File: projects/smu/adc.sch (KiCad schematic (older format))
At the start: 30 parts, among them P301 CONN_01X15, P302 CONN_01X03, U301 LM741, U304 LM741, U305 LM311N, U8 DG444, U9 LM741

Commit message: pulled out the connectors to the top sheet
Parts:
- removed P301: CONN_01X15, Pin_Headers:Pin_Header_Straight_1x15, symbol CONN_01X15
- removed P302: CONN_01X03, Pin_Headers:Pin_Header_Straight_1x03, symbol CONN_01X03
- added R307, R308: R, symbol R
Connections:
- wire segments 86 -> 69
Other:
- moved on the sheet: R306, U305
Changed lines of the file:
@@
 Text GLabel 2450 2900 0    60   Input ~ 0
 AGND
-Text GLabel 1750 800  2    60   Input ~ 0
-+VE
-Text GLabel 1750 900  2    60   Input ~ 0
-AGND
-Text GLabel 1750 1000 2    60   Input ~ 0
--VE
 Text GLabel 1650 2700 0    60   Input ~ 0
 REF
@@
 	0    1    1    0
 $EndComp
-Text GLabel 1750 1200 2    60   Input ~ 0
-REF
-Text GLabel 1750 1300 2    60   Input ~ 0
-IN
-Text GLabel 1750 1500 2    60   Input ~ 0
-3.3V
-Text GLabel 1750 1600 2    60   Input ~ 0
-REF_PLUS_CTL
-Text GLabel 1750 1700 2    60   Input ~ 0
-REF_SUB_CTL
-Text GLabel 1750 1800 2    60   Input ~ 0
-IN_CTL
-Text GLabel 1750 1900 2    60   Input ~ 0
-RESET
-$Comp
-L CONN_01X15 P301
-U 1 1 585C02F8
-P 1300 1500
-F 0 "P301" H 1300 2300 50  0000 C CNN
-F 1 "CONN_01X15" V 1400 1500 50  0000 C CNN
-F 2 "Pin_Headers:Pin_Header_Straight_1x15" H 1300 1500 50  0001 C CNN
-F 3 "" H 1300 1500 50  0000 C CNN
-	1    1300 1500
-	-1   0    0    -1
-$EndComp
-Text GLabel 1750 1100 2    60   Input ~ 0
-AGND
-Text GLabel 1750 1400 2    60   Input ~ 0
-AGND
 $Comp
 L LM741 U304
@@
 L LM311N U305
 U 1 1 5860DAF8
-P 9200 2200
-F 0 "U305" H 9200 2450 50  0000 L CNN
-F 1 "LM311N" H 9200 2350 50  0000 L CNN
-F 2 "Housings_SOIC:SOIC-8_3.9x4.9mm_Pitch1.27mm" H 9200 2200 50  0001 C CNN
-F 3 "" H 9200 2200 50  0000 C CNN
-	1    9200 2200
-	1    0    0    -1
-$EndComp
-Text GLabel 1750 2100 2    60   Input ~ 0
-AGND
-Text GLabel 1750 2200 2    60   Input ~ 0
-AGND
+P 9500 2200
+F 0 "U305" H 9500 2450 50  0000 L CNN
+F 1 "LM311N" H 9500 2350 50  0000 L CNN
+F 2 "Housings_SOIC:SOIC-8_3.9x4.9mm_Pitch1.27mm" H 9500 2200 50  0001 C CNN
+F 3 "" H 9500 2200 50  0000 C CNN
+	1    9500 2200
+	1    0    0    -1
+$EndComp
 $Comp
 L TEST_1P W301
@@
 	1    0    0    -1
 $EndComp
-Text GLabel 8700 2300 0    60   Input ~ 0
-AGND
-Text GLabel 9100 1700 1    60   Input ~ 0
+Text GLabel 9000 2300 0    60   Input ~ 0
+AGND
+Text GLabel 9400 1700 1    60   Input ~ 0
 +VE
-Text GLabel 9100 2750 3    60   Input ~ 0
+Text GLabel 9400 2750 3    60   Input ~ 0
 -VE
-Text GLabel 9200 2750 3    60   Input ~ 0
-AGND
-Text GLabel 9900 2200 2    60   Input ~ 0
+Text GLabel 9500 2750 3    60   Input ~ 0
+AGND
+Text GLabel 10200 2200 2    60   Input ~ 0
 TRIGGER
-Text GLabel 1750 2000 2    60   Input ~ 0
-TRIGGER
 Wire Wire Line
 	4100 2800 4450 2800
@@
 Wire Wire Line
 	2450 2900 2900 2900
-Wire Wire Line
-	1500 800  1750 800
-Wire Wire Line
-	1500 900  1750 900
-Wire Wire Line
-	1500 1000 1750 1000
 Wire Wire Line
 	4100 2600 4200 2600
@@
 Connection ~ 5550 2750
 Wire Wire Line
-	1500 1200 1750 1200
-Wire Wire Line
-	1500 1300 1750 1300
-Wire Wire Line
-	1500 1500 1750 1500
-Wire Wire Line
-	1500 1600 1750 1600
-Wire Wire Line
-	1500 1700 1750 1700
-Wire Wire Line
 	7750 1750 7750 1800
 Wire Wire Line
 	7750 2400 7750 2500
 Wire Wire Line
-	8150 2100 8500 2100
-Wire Wire Line
-	8750 2100 8900 2100
+	8150 2100 8450 2100
+Wire Wire Line
+	8750 2100 9200 2100
 Wire Wire Line
 	8300 2100 8300 3550
@@
 Connection ~ 8300 3250
 Wire Wire Line
-	8700 2300 8900 2300
-Wire Wire Line
-	9100 1700 9100 1900
-Wire Wire Line
-	9100 2500 9100 2750
-Wire Wire Line
-	9500 2200 9900 2200
-Wire Wire Line
-	9200 2500 9200 2750
-Wire Wire Line
-	1500 1100 1750 1100
-Wire Wire Line
-	1500 1400 1750 1400
-Wire Wire Line
-	1500 1800 1750 1800
-Wire Wire Line
-	1500 1900 1750 1900
-Wire Wire Line
-	1500 2000 1750 2000
-Wire Wire Line
-	1500 2100 1750 2100
-Wire Wire Line
-	1750 2200 1500 2200
-NoConn ~ 9500 2300
-NoConn ~ 9300 2500
+	9000 2300 9200 2300
+Wire Wire Line
+	9400 1700 9400 1900
+Wire Wire Line
+	9400 2500 9400 2750
+Wire Wire Line
+	9800 2200 10200 2200
+Wire Wire Line
+	9500 2500 9500 2750
+NoConn ~ 9800 2300
+NoConn ~ 9600 2500
 NoConn ~ 7950 2400
 NoConn ~ 7850 2400
@@
 L R R306
 U 1 1 58620487
-P 9750 1850
-F 0 "R306" V 9830 1850 50  0000 C CNN
-F 1 "5k" V 9750 1850 50  0000 C CNN
-F 2 "Resistors_SMD:R_1206" V 9680 1850 50  0001 C CNN
-F 3 "" H 9750 1850 50  0000 C CNN
-	1    9750 1850
-	1    0    0    -1
-$EndComp
-Wire Wire Line
-	9750 2000 9750 2200
-Connection ~ 9750 2200
-Text GLabel 9750 1550 1    60   Input ~ 0
+P 10050 1850
+F 0 "R306" V 10130 1850 50  0000 C CNN
+F 1 "5k" V 10050 1850 50  0000 C CNN
+F 2 "Resistors_SMD:R_1206" V 9980 1850 50  0001 C CNN
+F 3 "" H 10050 1850 50  0000 C CNN
+	1    10050 1850
+	1    0    0    -1
+$EndComp
+Wire Wire Line
+	10050 2000 10050 2200
+Connection ~ 10050 2200
+Text GLabel 10050 1550 1    60   Input ~ 0
 +VE
 Wire Wire Line
-	9750 1550 9750 1700
-$Comp
-L CONN_01X03 P302
-U 1 1 58621C5B
-P 9100 950
-F 0 "P302" H 9100 1150 50  0000 C CNN
-F 1 "CONN_01X03" V 9200 950 50  0000 C CNN
-F 2 "Pin_Headers:Pin_Header_Straight_1x03" H 9100 950 50  0001 C CNN
-F 3 "" H 9100 950 50  0000 C CNN
-	1    9100 950
-	1    0    0    -1
-$EndComp
-Wire Wire Line
-	7100 2000 7100 850
-Wire Wire Line
-	7100 850  8900 850
-Connection ~ 7100 2000
-Wire Wire Line
-	8900 950  8750 950
-Wire Wire Line
-	8750 950  8750 2100
-Wire Wire Line
-	8900 1050 8500 1050
-Wire Wire Line
-	8500 1050 8500 2100
+	10050 1550 10050 1700
+Connection ~ 7350 2000
 $Comp
 L C C314
@@
 	6300 3000 6750 3000
 Connection ~ 6750 3000
+$Comp
+L R R307
+U 1 1 58A9778D
+P 8600 2100
+F 0 "R307" V 8680 2100 50  0000 C CNN
+F 1 "R" V 8600 2100 50  0000 C CNN
+F 2 "" V 8530 2100 50  0000 C CNN
+F 3 "" H 8600 2100 50  0000 C CNN
+	1    8600 2100
+	0    1    1    0
+$EndComp
+$Comp
+L R R308
+U 1 1 58A97AC8
+P 8600 1350
+F 0 "R308" V 8680 1350 50  0000 C CNN
+F 1 "R" V 8600 1350 50  0000 C CNN
+F 2 "" V 8530 1350 50  0000 C CNN
+F 3 "" H 8600 1350 50  0000 C CNN
+	1    8600 1350
+	0    1    1    0
+$EndComp
+Wire Wire Line
+	8450 1350 7350 1350
+Wire Wire Line
+	8750 1350 8900 1350
+Wire Wire Line
+	8900 1350 8900 2100
+Connection ~ 8900 2100
+Wire Wire Line
+	7350 1350 7350 2000
 $EndSCHEMATC

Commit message: generate net and parts
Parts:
- R307, R308: footprint (none) -> Resistors_SMD:R_1206
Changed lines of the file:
@@
 F 0 "R307" V 8680 2100 50  0000 C CNN
 F 1 "R" V 8600 2100 50  0000 C CNN
-F 2 "" V 8530 2100 50  0000 C CNN
+F 2 "Resistors_SMD:R_1206" V 8530 2100 50  0001 C CNN
 F 3 "" H 8600 2100 50  0000 C CNN
 	1    8600 2100
@@
 F 0 "R308" V 8680 1350 50  0000 C CNN
 F 1 "R" V 8600 1350 50  0000 C CNN
-F 2 "" V 8530 1350 50  0000 C CNN
+F 2 "Resistors_SMD:R_1206" V 8530 1350 50  0001 C CNN
 F 3 "" H 8600 1350 50  0000 C CNN
 	1    8600 1350

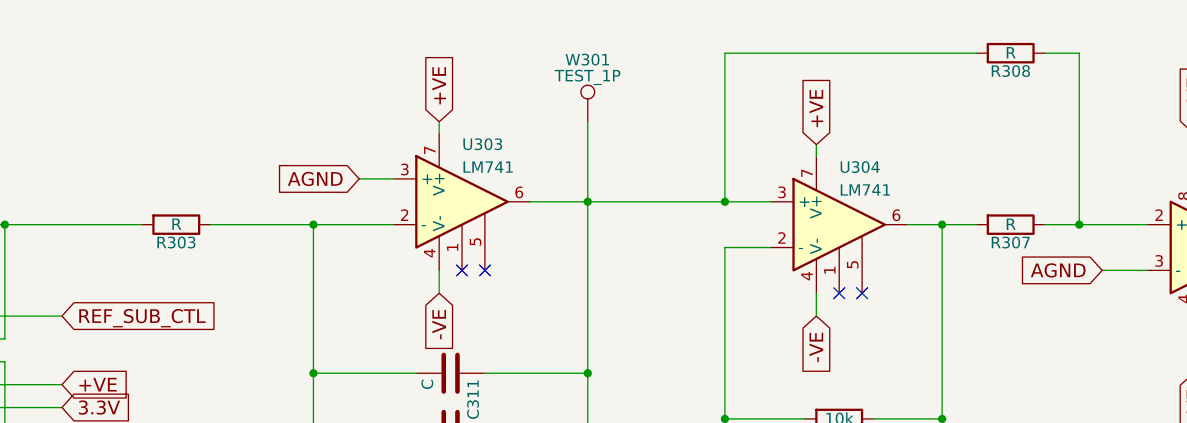
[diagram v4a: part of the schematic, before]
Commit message: change resistors to all 1206
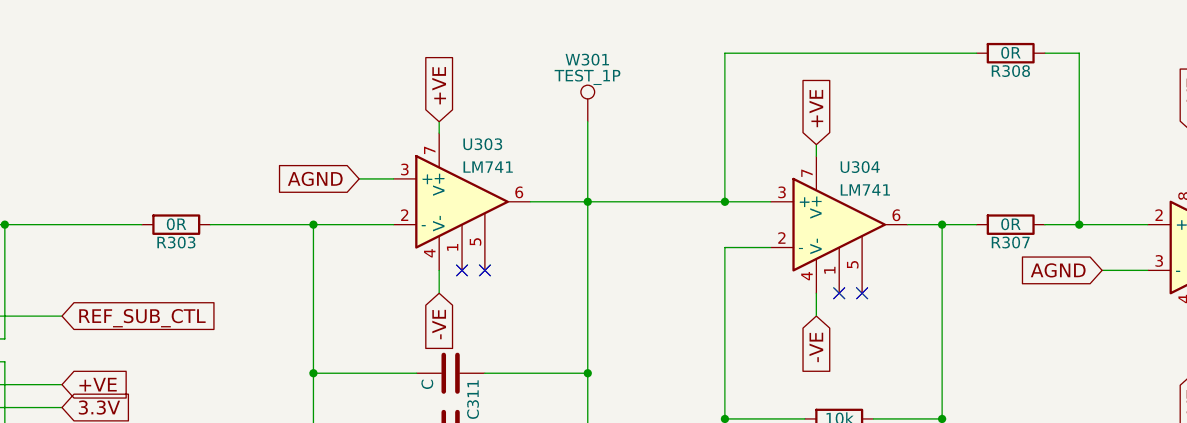
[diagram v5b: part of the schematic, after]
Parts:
- R16, R307, R308: value R -> 0R
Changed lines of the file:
@@
 AR Path="/58843A43/585BA8B1" Ref="R303"  Part="1"
 F 0 "R303" V 5030 2100 50  0000 C CNN
-F 1 "R" V 4950 2100 50  0000 C CNN
+F 1 "0R" V 4950 2100 50  0000 C CNN
 F 2 "Resistors_ThroughHole:Resistor_TO-220_Vertical" V 4880 2100 50  0001 C CNN
 F 3 "" H 4950 2100 50  0000 C CNN
@@
 P 8600 2100
 F 0 "R307" V 8680 2100 50  0000 C CNN
-F 1 "R" V 8600 2100 50  0000 C CNN
+F 1 "0R" V 8600 2100 50  0000 C CNN
 F 2 "Resistors_SMD:R_1206" V 8530 2100 50  0001 C CNN
 F 3 "" H 8600 2100 50  0000 C CNN
@@
 P 8600 1350
 F 0 "R308" V 8680 1350 50  0000 C CNN
-F 1 "R" V 8600 1350 50  0000 C CNN
+F 1 "0R" V 8600 1350 50  0000 C CNN
 F 2 "Resistors_SMD:R_1206" V 8530 1350 50  0001 C CNN
 F 3 "" H 8600 1350 50  0000 C CNN

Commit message: do edges again
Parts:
- R16, R301, R302: footprint Resistors_ThroughHole:Resistor_TO-220_Vertical -> Resistors_SMD:R_1206
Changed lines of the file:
@@
 F 0 "R303" V 5030 2100 50  0000 C CNN
 F 1 "0R" V 4950 2100 50  0000 C CNN
-F 2 "Resistors_ThroughHole:Resistor_TO-220_Vertical" V 4880 2100 50  0001 C CNN
+F 2 "Resistors_SMD:R_1206" V 4880 2100 50  0001 C CNN
 F 3 "" H 4950 2100 50  0000 C CNN
 	1    4950 2100
@@
 F 0 "R302" V 3530 4850 50  0000 C CNN
 F 1 "R" V 3450 4850 50  0000 C CNN
-F 2 "Resistors_ThroughHole:Resistor_TO-220_Vertical" V 3380 4850 50  0001 C CNN
+F 2 "Resistors_SMD:R_1206" V 3380 4850 50  0001 C CNN
 F 3 "" H 3450 4850 50  0000 C CNN
 	1    3450 4850
@@
 F 0 "R301" V 2780 4300 50  0000 C CNN
 F 1 "R" V 2700 4300 50  0000 C CNN
-F 2 "Resistors_ThroughHole:Resistor_TO-220_Vertical" V 2630 4300 50  0001 C CNN
+F 2 "Resistors_SMD:R_1206" V 2630 4300 50  0001 C CNN
 F 3 "" H 2700 4300 50  0000 C CNN
 	1    2700 4300
